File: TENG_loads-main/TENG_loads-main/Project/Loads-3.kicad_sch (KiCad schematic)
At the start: 24 parts, among them K33 V23079C1103B301, K34 V23079C1103B301, K35 V23079C1103B301, K36 V23079C1103B301, K37 V23079C1103B301, K38 IMC03TS, K39 IMC03TS, K40 IMC03TS, K41 IMC03TS, K42 IMC03TS, K43 V23079C1103B301, K44 V23079C1103B301, K45 V23079C1103B301, K46 IMC03TS, K47 IMC03TS, K48 IMC03TS

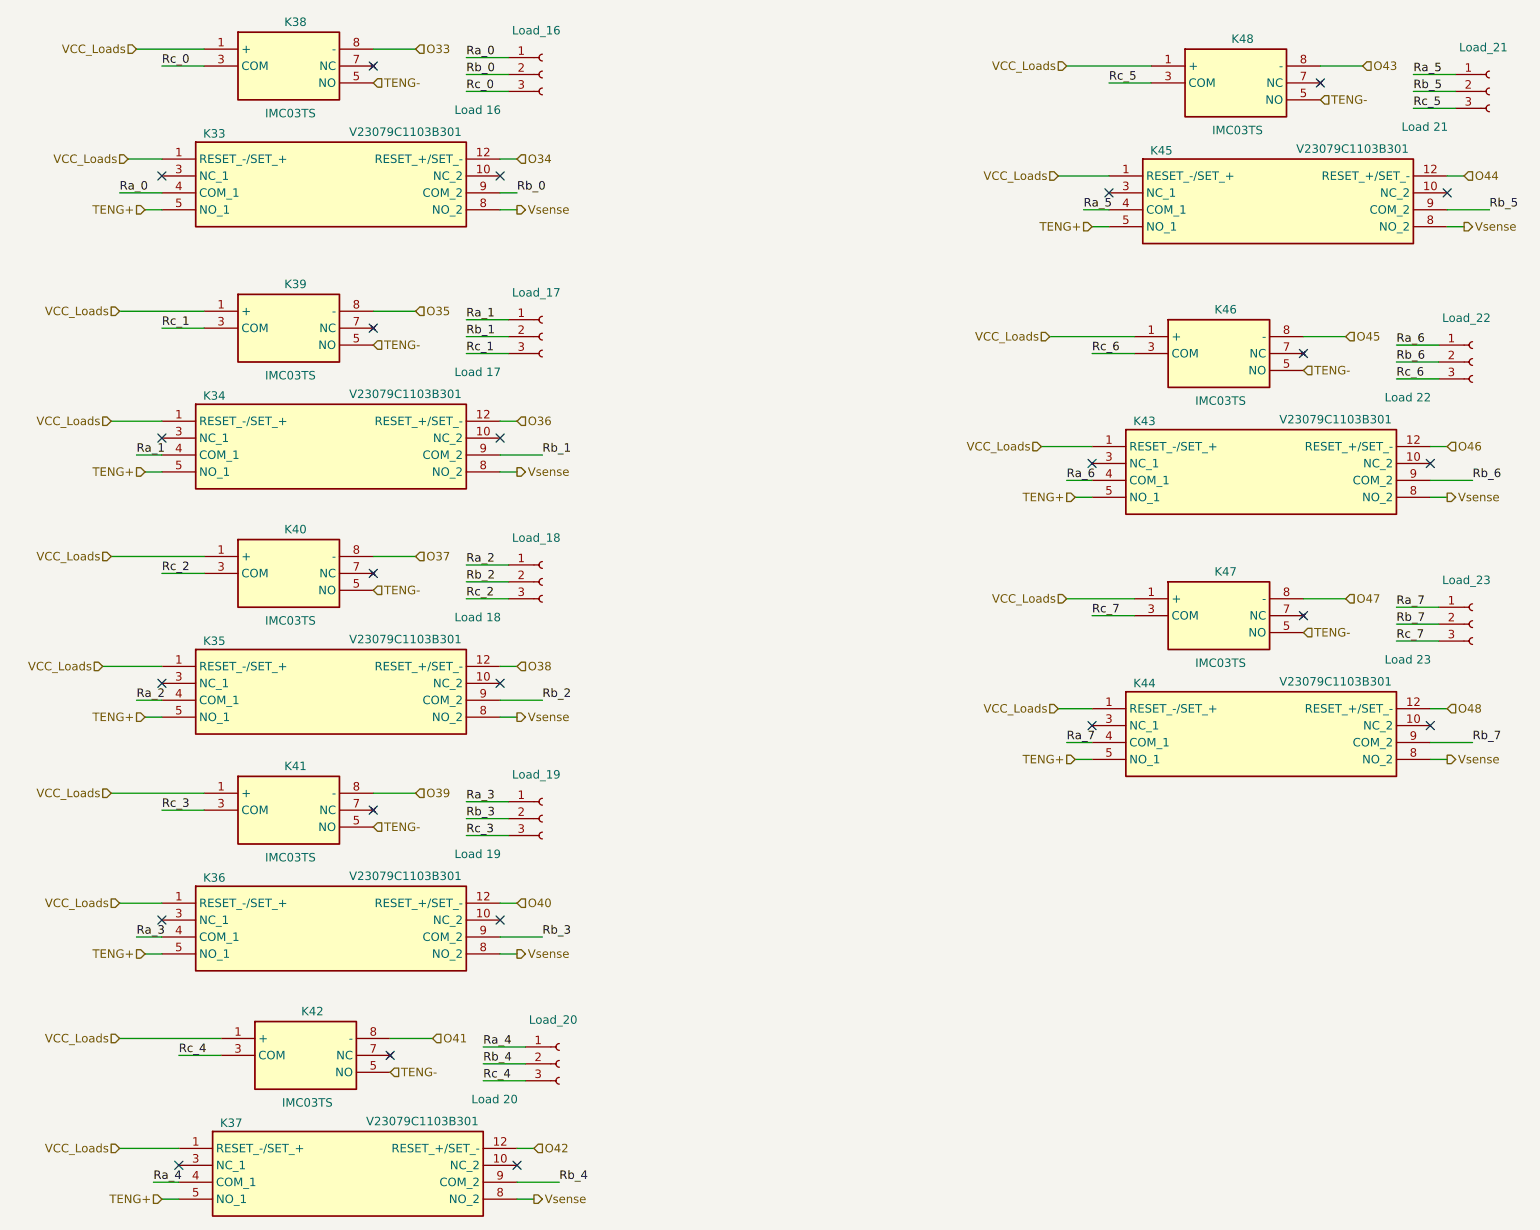
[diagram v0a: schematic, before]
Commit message: Changed Relay identifier
Changed relay identifier with the correct one (12 VDC changed to 5 VDC).
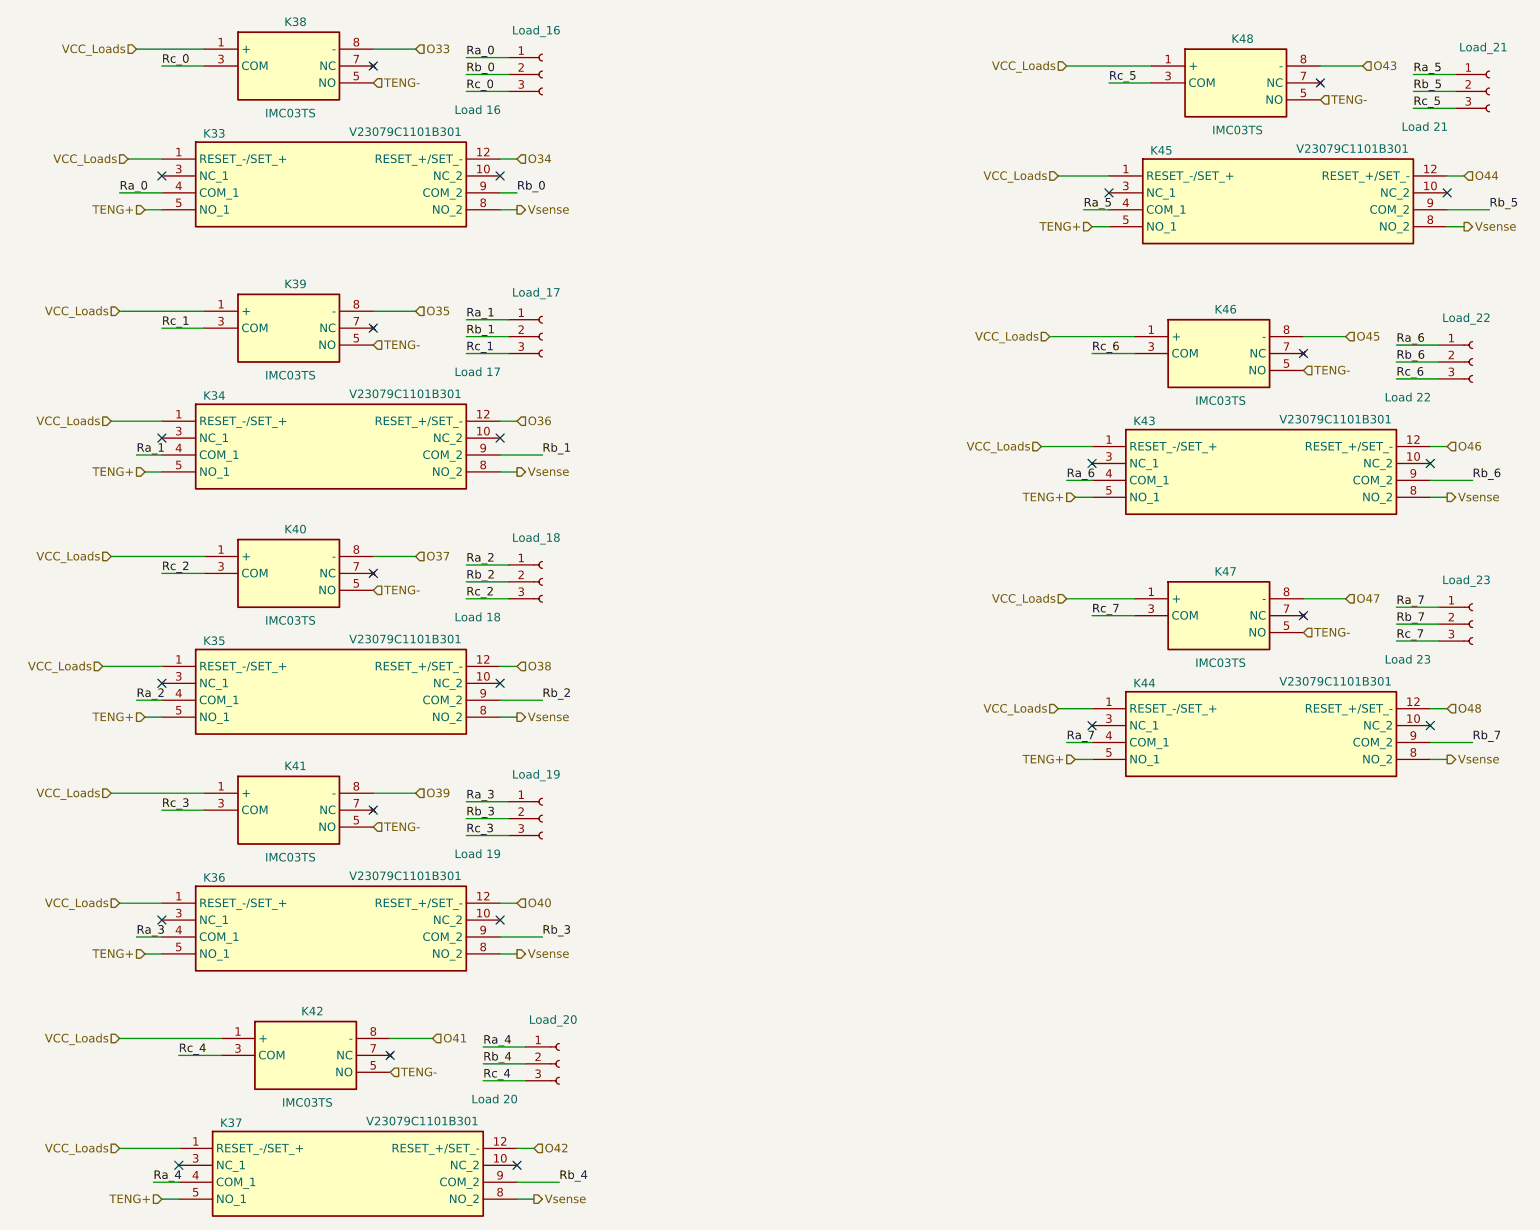
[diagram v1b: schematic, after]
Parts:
- K33, K34, K35, K36, K37, K43, K44, K45: value V23079C1103B301 -> V23079C1101B301
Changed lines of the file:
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@@
 			)
 		)
-		(property "Value" "V23079C1103B301"
+		(property "Value" "V23079C1101B301"
 			(at 105.156 72.136 0)
 			(effects
@@
 			)
 		)
-		(property "Value" "V23079C1103B301"
+		(property "Value" "V23079C1101B301"
 			(at 107.696 181.356 0)
 			(effects
@@
 			)
 		)
-		(property "Value" "V23079C1103B301"
+		(property "Value" "V23079C1101B301"
 			(at 244.856 115.316 0)
 			(effects
@@
 			)
 		)
-		(property "Value" "V23079C1103B301"
+		(property "Value" "V23079C1101B301"
 			(at 105.156 144.526 0)
 			(effects
@@
 			)
 		)
-		(property "Value" "V23079C1103B301"
+		(property "Value" "V23079C1101B301"
 			(at 247.396 35.306 0)
 			(effects
@@
 			)
 		)
-		(property "Value" "V23079C1103B301"
+		(property "Value" "V23079C1101B301"
 			(at 244.856 75.946 0)
 			(effects
@@
 			)
 		)
-		(property "Value" "V23079C1103B301"
+		(property "Value" "V23079C1101B301"
 			(at 105.156 108.966 0)
 			(effects
@@
 			)
 		)
-		(property "Value" "V23079C1103B301"
+		(property "Value" "V23079C1101B301"
 			(at 105.156 32.766 0)
 			(effects

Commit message: Capacitor and relay changes
Capacitor correction and relay ID correction
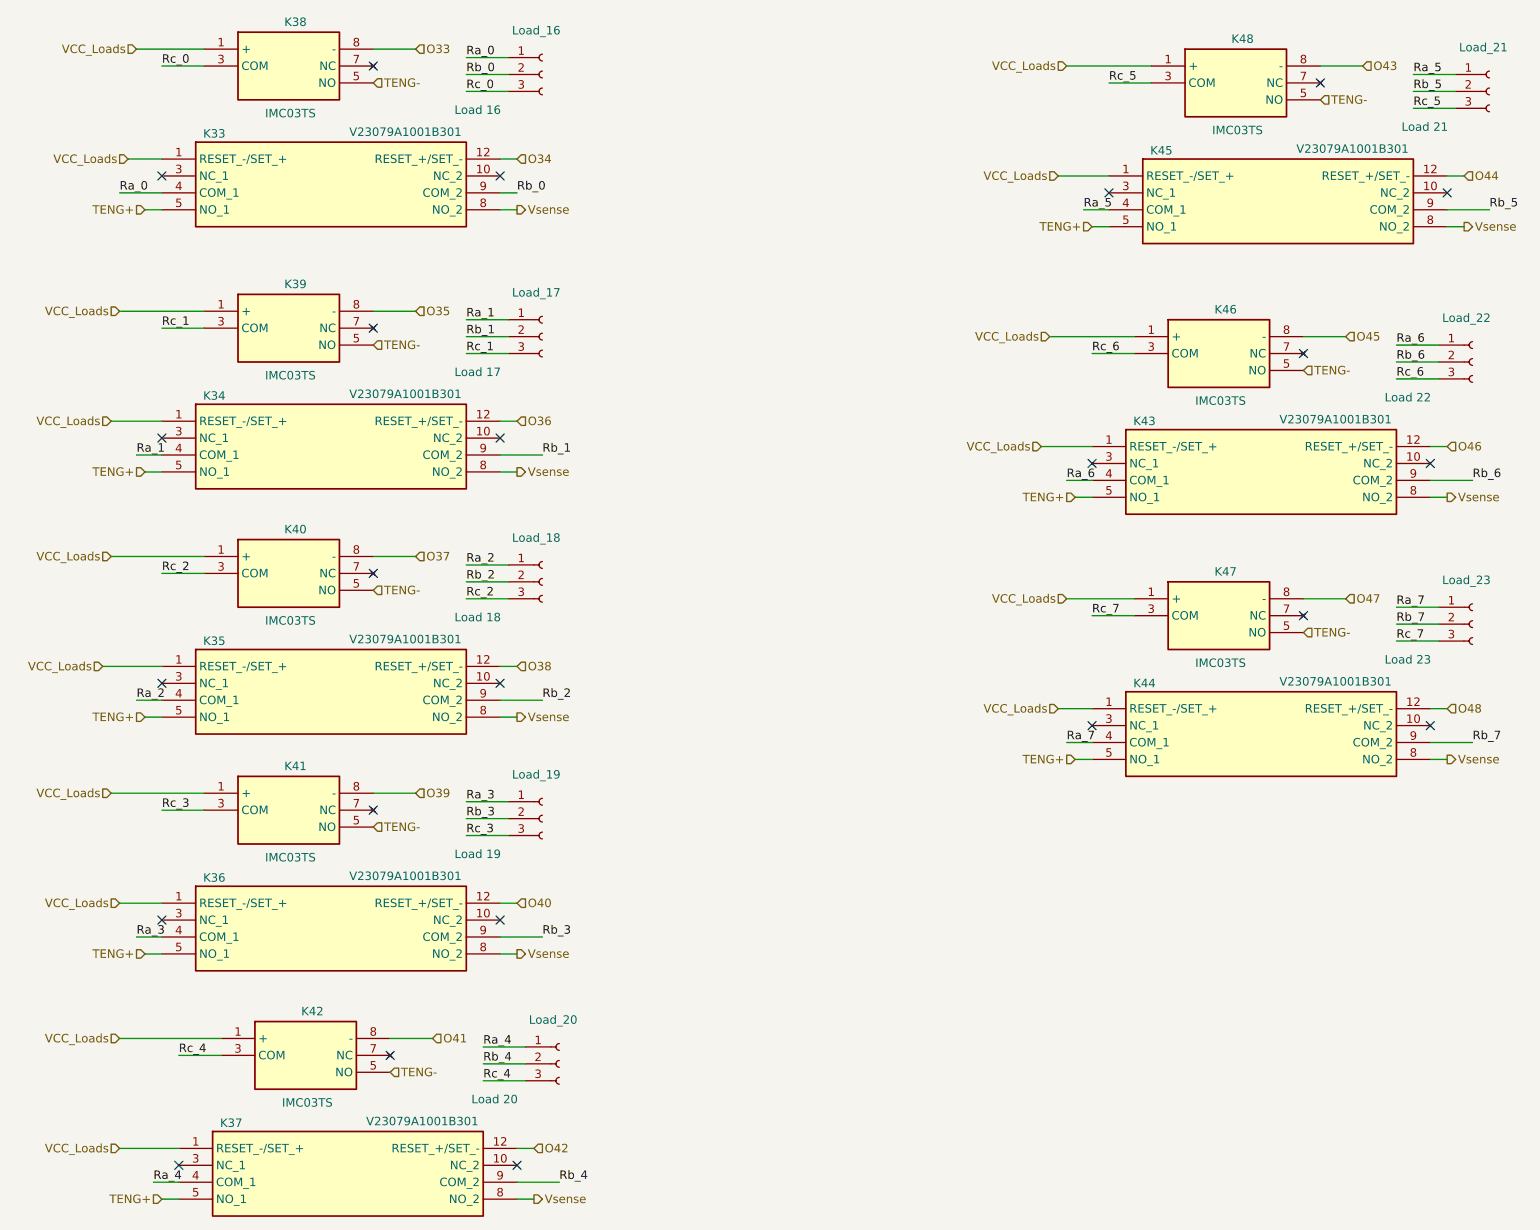
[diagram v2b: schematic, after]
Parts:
- K33, K34, K35, K36, K37, K43, K44, K45: value V23079C1101B301 -> V23079A1001B301
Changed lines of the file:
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@@
 			)
 		)
-		(property "Value" "V23079C1101B301"
+		(property "Value" "V23079A1001B301"
 			(at 105.156 72.136 0)
 			(effects
@@
 			)
 		)
-		(property "Value" "V23079C1101B301"
+		(property "Value" "V23079A1001B301"
 			(at 107.696 181.356 0)
 			(effects
@@
 			)
 		)
-		(property "Value" "V23079C1101B301"
+		(property "Value" "V23079A1001B301"
 			(at 244.856 115.316 0)
 			(effects
@@
 			)
 		)
-		(property "Value" "V23079C1101B301"
+		(property "Value" "V23079A1001B301"
 			(at 105.156 144.526 0)
 			(effects
@@
 			)
 		)
-		(property "Value" "V23079C1101B301"
+		(property "Value" "V23079A1001B301"
 			(at 247.396 35.306 0)
 			(effects
@@
 			)
 		)
-		(property "Value" "V23079C1101B301"
+		(property "Value" "V23079A1001B301"
 			(at 244.856 75.946 0)
 			(effects
@@
 			)
 		)
-		(property "Value" "V23079C1101B301"
+		(property "Value" "V23079A1001B301"
 			(at 105.156 108.966 0)
 			(effects
@@
 			)
 		)
-		(property "Value" "V23079C1101B301"
+		(property "Value" "V23079A1001B301"
 			(at 105.156 32.766 0)
 			(effects
